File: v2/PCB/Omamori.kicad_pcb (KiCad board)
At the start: 2 copper layers, 26 x 36 mm, 12 parts, among them U1 BQ25504, U2 ATtiny13A-SSU

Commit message: Modified PCB and updated Software.
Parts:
- added D10: BPW34, own_footprints:Osram_DIL2_4.3x4.65mm_P5.08mm, F.Cu at (180.2, 91.0)
- added D11: BPW34, own_footprints:Osram_DIL2_4.3x4.65mm_P5.08mm, F.Cu at (190.2, 90.8)
- added D12: BPW34, own_footprints:Osram_DIL2_4.3x4.65mm_P5.08mm, F.Cu at (179.8, 106.8)
- added D13: BPW34, own_footprints:Osram_DIL2_4.3x4.65mm_P5.08mm, F.Cu at (187.8, 95.8)
- added D14: BPW34, own_footprints:Osram_DIL2_4.3x4.65mm_P5.08mm, F.Cu at (169.8, 111.2)
- added D15: BPW34, own_footprints:Osram_DIL2_4.3x4.65mm_P5.08mm, F.Cu at (187.8, 106.2)
- added D16: BPW34, own_footprints:Osram_DIL2_4.3x4.65mm_P5.08mm, F.Cu at (172.2, 106.2)
- added D17: BPW34, own_footprints:Osram_DIL2_4.3x4.65mm_P5.08mm, F.Cu at (177.2, 111.5)
- added D18: BPW34, own_footprints:Osram_DIL2_4.3x4.65mm_P5.08mm, F.Cu at (179.8, 91.0)
- added D19: BPW34, own_footprints:Osram_DIL2_4.3x4.65mm_P5.08mm, F.Cu at (172.2, 95.8)
- added D20: BPW34, own_footprints:Osram_DIL2_4.3x4.65mm_P5.08mm, F.Cu at (177.2, 86.2)
- added D21: BPW34, own_footprints:Osram_DIL2_4.3x4.65mm_P5.08mm, F.Cu at (182.8, 86.2)
- CSuper1: footprint Capacitor_THT:C_Rect_L7.2mm_W2.5mm_P5.00mm_FKS2_FKP2_MKS2_MKP2 -> Capacitor_THT:C_Radial_D10.0mm_H12.5mm_P5.00mm
- D1, D2, D3, D4, D5, D6, D7, D8: footprint OptoDevice:Osram_DIL2_4.3x4.65mm_P5.08mm -> own_footprints:Osram_DIL2_4.3x4.65mm_P5.08mm
- D9: footprint LED_SMD:LED_WS2812B_PLCC4_5.0x5.0mm_P3.2mm -> LED_SMD:LED_SK6812_PLCC4_5.0x5.0mm_P3.2mm
- moved D8 23.2 mm to (182.8, 111.5), turned to 0 degrees
- moved D6 11.3 mm to (190.2, 111.2), turned to 90 degrees
- moved D7 9.28 mm to (190.2, 101.0), turned to 90 degrees
- moved D3 7.52 mm to (174.8, 101.0), turned to 90 degrees
- moved D5 7.52 mm to (185.2, 101.0), turned to 90 degrees
- moved D4 4.76 mm to (180.2, 106.8), turned to 0 degrees
- moved D1 2.57 mm to (169.8, 90.8), turned to 90 degrees
- moved U2 2.30 mm to (185.2, 88.8), turned to 270 degrees
- moved D2 1.60 mm to (169.8, 101.0), turned to 90 degrees
- moved CSuper1 1.50 mm to (180.0, 101.0)
- moved D9 1.50 mm to (180.0, 98.5)
- moved U1 0.56 mm to (174.8, 87.5)
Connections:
- D1 pad 2: Net-(D1-Pad2) -> GND
- D2 pad 1: Net-(D1-Pad2) -> Net-(D1-Pad1)
- D2 pad 2: Net-(D2-Pad2) -> GND
- D3 pad 1: Net-(D2-Pad2) -> Net-(D1-Pad1)
- D3 pad 2: Net-(D3-Pad2) -> GND
- D4 pad 1: Net-(D3-Pad2) -> Net-(D1-Pad1)
- D4 pad 2: Net-(D4-Pad2) -> GND
- D5 pad 1: Net-(D4-Pad2) -> Net-(D1-Pad1)
- D5 pad 2: Net-(D5-Pad2) -> GND
- D6 pad 1: Net-(D5-Pad2) -> Net-(D1-Pad1)
- D6 pad 2: Net-(D6-Pad2) -> GND
- D7 pad 1: Net-(D6-Pad2) -> Net-(D1-Pad1)
- D7 pad 2: Net-(D7-Pad2) -> GND
- D8 pad 1: Net-(D7-Pad2) -> Net-(D1-Pad1)
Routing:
- net GND: track 26.7 -> 140.2 mm
- net Net-(CSuper1-Pad1): track 15.0 -> 0.00 mm
- net Net-(D1-Pad1): track 0.00 -> 11.6 mm
- net Net-(D5-Pad2): track 8.92 -> 0.00 mm
- net Net-(D1-Pad2): track 8.92 -> 0.00 mm
- net Net-(D7-Pad2): track 8.92 -> 0.00 mm
- net Net-(D3-Pad2): track 8.92 -> 0.00 mm
- net Net-(D6-Pad2): track 8.65 -> 0.00 mm
- net Net-(D2-Pad2): track 8.65 -> 0.00 mm
- net Net-(D4-Pad2): track 8.65 -> 0.00 mm

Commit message: Updated version 2 PCB.
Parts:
- removed the D1 at (169.8, 90.8)
- removed D10, D11, D12, D13, D14, D15, D16, D17, D18, D19, D2, D20, D21, D3, D4, D5, D6, D7, D8: BPW34, own_footprints:Osram_DIL2_4.3x4.65mm_P5.08mm
- added C_filter1: 0.1uF, Capacitor_SMD:C_0603_1608Metric_Pad1.05x0.95mm_HandSolder, B.Cu at (27.0, 24.0)
- added C_hvr1: 4.7uF, Capacitor_SMD:C_0603_1608Metric_Pad1.05x0.95mm_HandSolder, B.Cu at (32.0, 16.5)
- added C_led1: 100nF, Capacitor_SMD:C_0603_1608Metric_Pad1.05x0.95mm_HandSolder, B.Cu at (15.0, 36.0)
- added C_post_boost1: 10uF, Capacitor_SMD:C_0603_1608Metric_Pad1.05x0.95mm_HandSolder, B.Cu at (15.0, 20.0)
- added C_pre_boost1: 10uF, Capacitor_SMD:C_0603_1608Metric_Pad1.05x0.95mm_HandSolder, B.Cu at (21.0, 22.2)
- added C_ref1: 0.01uF, Capacitor_SMD:C_0603_1608Metric_Pad1.05x0.95mm_HandSolder, B.Cu at (35.0, 21.5)
- added J1: Conn_01x04_Female, Connector_PinHeader_1.27mm:PinHeader_1x04_P1.27mm_Horizontal, B.Cu at (27.0, 46.5)
- added L_boost1: 4.7uH, Inductor_SMD:L_Wuerth_MAPI-3015, B.Cu at (21.5, 18.5)
- added L_bst1: 22uH, Inductor_SMD:L_Wuerth_MAPI-3015, B.Cu at (27.8, 18.5)
- added R1: 1M, Resistor_SMD:R_0603_1608Metric_Pad1.05x0.95mm_HandSolder, B.Cu at (16.1, 17.0)
- added R_data1: 500, Resistor_SMD:R_0603_1608Metric_Pad1.05x0.95mm_HandSolder, B.Cu at (15.0, 32.5)
- added R_oc1: 3.9M, Resistor_SMD:R_0603_1608Metric_Pad1.05x0.95mm_HandSolder, B.Cu at (32.0, 19.8)
- added R_oc2: 6.2M, Resistor_SMD:R_0603_1608Metric_Pad1.05x0.95mm_HandSolder, B.Cu at (32.0, 18.0)
- added R_ok1: 2.4M, Resistor_SMD:R_0603_1608Metric_Pad1.05x0.95mm_HandSolder, B.Cu at (34.0, 29.0)
- added R_ok2: 1.6M, Resistor_SMD:R_0603_1608Metric_Pad1.05x0.95mm_HandSolder, B.Cu at (31.5, 28.0)
- added R_ok3: 6.2M, Resistor_SMD:R_0603_1608Metric_Pad1.05x0.95mm_HandSolder, B.Cu at (30.0, 28.0)
- added R_ov1: 6.2M, Resistor_SMD:R_0603_1608Metric_Pad1.05x0.95mm_HandSolder, B.Cu at (34.0, 24.5)
- added R_ov2: 3.3M, Resistor_SMD:R_0603_1608Metric_Pad1.05x0.95mm_HandSolder, B.Cu at (34.0, 23.0)
- added R_uv1: 1.6M, Resistor_SMD:R_0603_1608Metric_Pad1.05x0.95mm_HandSolder, B.Cu at (34.0, 26.0)
- added R_uv2: 8.2M, Resistor_SMD:R_0603_1608Metric_Pad1.05x0.95mm_HandSolder, B.Cu at (34.0, 27.5)
- added Sol_1: KXOB25-05X3F, own_footprints:KXOB25-05X3F, F.Cu at (33.0, 30.0)
- added Sol_2: KXOB25-05X3F, own_footprints:KXOB25-05X3F, F.Cu at (17.0, 30.0)
- added U2: TPS61222DCK, Package_TO_SOT_SMD:Texas_R-PDSO-G6, B.Cu at (18.0, 20.0)
- C_super1: renamed from CSuper1; value C -> 640mF; footprint Capacitor_THT:C_Radial_D10.0mm_H12.5mm_P5.00mm -> own_footprints:Supercap
- moved U3 179.4 mm to (17.0, 26.5), turned to 90 degrees
- moved D1 169.3 mm to (25.0, 30.5)
- moved C_super1 167.7 mm to (25.0, 37.0), turned to 180 degrees
- moved U1 158.4 mm to (30.1, 22.9), turned to 270 degrees
- renumbered D9 to D1, U2 to U3
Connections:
- D1 pad 2: Net-(D9-Pad2) -> Net-(D1-Pad2)
- D1 pad 3: Net-(D9-Pad3) -> Net-(C_led1-Pad1)
- U1 pad 15: Net-(U1-Pad15) -> Net-(C_pre_boost1-Pad1)
- U1 pad 17: Net-(U1-Pad17) -> GND
- U1 pad 5: Net-(U1-Pad5) -> GND
- U3 pad 2: Net-(U2-Pad2) -> Net-(C_led1-Pad1)
- U3 pad 5: Net-(D9-Pad2) -> Net-(R1-Pad1)
- U3 pad 6: Net-(U1-Pad11) -> Net-(J1-Pad3)
- U3 pad 7: Net-(D9-Pad3) -> Net-(J1-Pad2)
- U3 pad 8: Net-(U1-Pad15) -> Net-(C_post_boost1-Pad1)
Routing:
- net Net-(Sol_1-Pad2): track 0.00 -> 34.5 mm
- net Net-(C_post_boost1-Pad1): track 0.00 -> 34.0 mm
- net GND: track 140.2 -> 106.9 mm, vias 0 -> 5
- net Net-(J1-Pad3): track 0.00 -> 26.5 mm
- net Net-(J1-Pad2): track 0.00 -> 25.8 mm
- net Net-(C_filter1-Pad1): track 0.00 -> 20.0 mm
- net Net-(C_hvr1-Pad1): track 11.6 -> 31.0 mm, vias 0 -> 1
- net Net-(U1-Pad11): track 0.00 -> 15.5 mm, vias 0 -> 2
- net Net-(C_pre_boost1-Pad1): track 0.00 -> 14.4 mm
- net Net-(C_led1-Pad1): track 0.00 -> 13.4 mm, vias 0 -> 1
- net Net-(D1-Pad2): track 0.00 -> 11.4 mm, vias 0 -> 1
- net Net-(R_ok1-Pad1): track 0.00 -> 8.90 mm
- net Net-(R1-Pad1): track 0.00 -> 7.83 mm
- net Net-(L_boost1-Pad2): track 0.00 -> 6.20 mm
- net Net-(R_ok1-Pad2): track 0.00 -> 5.53 mm
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
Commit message: Updated PCB layout and added gerber and pictures.
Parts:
- removed R1: 1M, Resistor_SMD:R_0603_1608Metric_Pad1.05x0.95mm_HandSolder
- added D2: DIODE, Diode_SMD:D_SOD-323_HandSoldering, B.Cu at (15.5, 17.0)
- U3: value ATtiny13A-SSU -> ATtiny85
- moved C_led1 13.3 mm to (23.8, 26.0), turned to 0 degrees
- moved R_data1 9.65 mm to (23.2, 27.5), turned to 180 degrees
- moved U3 1.03 mm to (18.0, 26.8), turned to 180 degrees
- moved C_post_boost1 1.00 mm to (16.0, 20.0)
- moved C_filter1 0.90 mm to (26.2, 23.5)
- moved L_boost1 0.35 mm to (21.8, 18.8)
- moved L_bst1 0.35 mm to (27.5, 18.8), turned to 270 degrees
- moved C_pre_boost1 0.25 mm to (21.0, 22.5)
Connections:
- net Net-(C_hvr1-Pad1) renamed /Vsolar
- net Net-(C_led1-Pad1) renamed /Vcc_LED
- net Net-(C_post_boost1-Pad1) renamed /Vcc_ATTiny
- net Net-(D1-Pad2) renamed /Din_LED
- net Net-(J1-Pad2) renamed /Rx
- net Net-(J1-Pad3) renamed /Tx
- net Net-(R_data1-Pad2) renamed /Data_LED
- net Net-(R_ok1-Pad1) renamed /Vr_div
- net Net-(U1-Pad11) renamed /Vbat_ok
- C_filter1 pad 1: Net-(C_filter1-Pad1) -> /Vstor
- C_pre_boost1 pad 1: Net-(C_pre_boost1-Pad1) -> /Vstor
- C_super1 pad 1: Net-(C_filter1-Pad1) -> Net-(C_super1-Pad1)
- L_boost1 pad 1: Net-(C_pre_boost1-Pad1) -> /Vstor
- U1 pad 14: Net-(C_filter1-Pad1) -> Net-(C_super1-Pad1)
- U1 pad 15: Net-(C_pre_boost1-Pad1) -> /Vstor
- U2 pad 1: Net-(C_pre_boost1-Pad1) -> /Vstor
- U3 pad 5: Net-(R1-Pad1) -> /Vsolar_measure
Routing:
- net Net-(C_filter1-Pad1): track 20.0 -> 0.00 mm
- net Net-(C_super1-Pad1): track 0.00 -> 17.1 mm
- net Net-(C_pre_boost1-Pad1): track 14.4 -> 0.00 mm
- net /Vstor: track 0.00 -> 14.0 mm
- net /Vsolar_measure: track 0.00 -> 13.4 mm
- net /Din_LED: track 11.4 -> 3.20 mm
- net Net-(R1-Pad1): track 7.83 -> 0.00 mm
- net GND: track 106.9 -> 112.0 mm, vias 5 -> 6
- net /Vsolar: track 31.0 -> 27.8 mm
- net /Tx: track 26.5 -> 23.4 mm
- net /Vcc_LED: track 13.4 -> 15.9 mm
- net /Vcc_ATTiny: track 34.0 -> 35.9 mm
- net Net-(L_boost1-Pad2): track 6.20 -> 4.59 mm
- net /Data_LED: track 3.49 -> 1.95 mm
- net Net-(Sol_1-Pad2): track 34.5 -> 33.7 mm
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
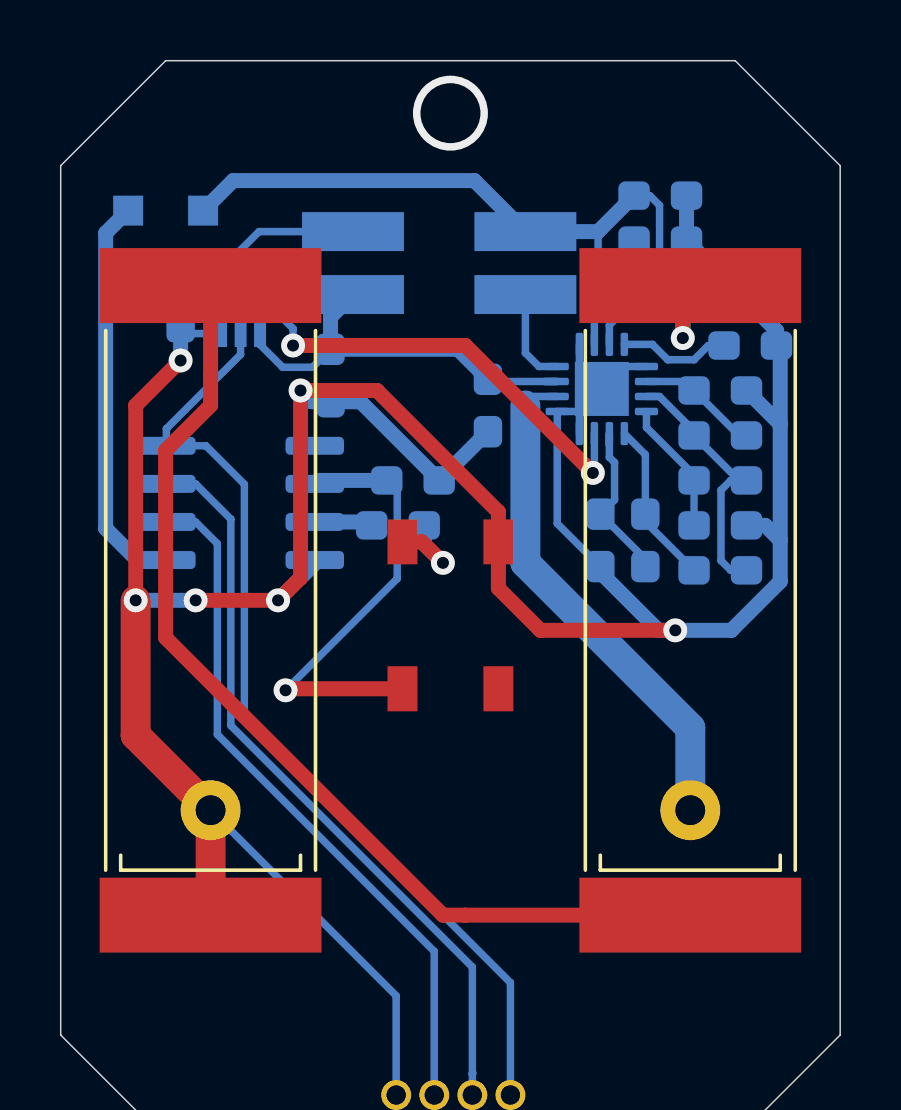
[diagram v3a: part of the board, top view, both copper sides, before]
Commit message: Thickened a lot of wires and ordered stuff a bit.
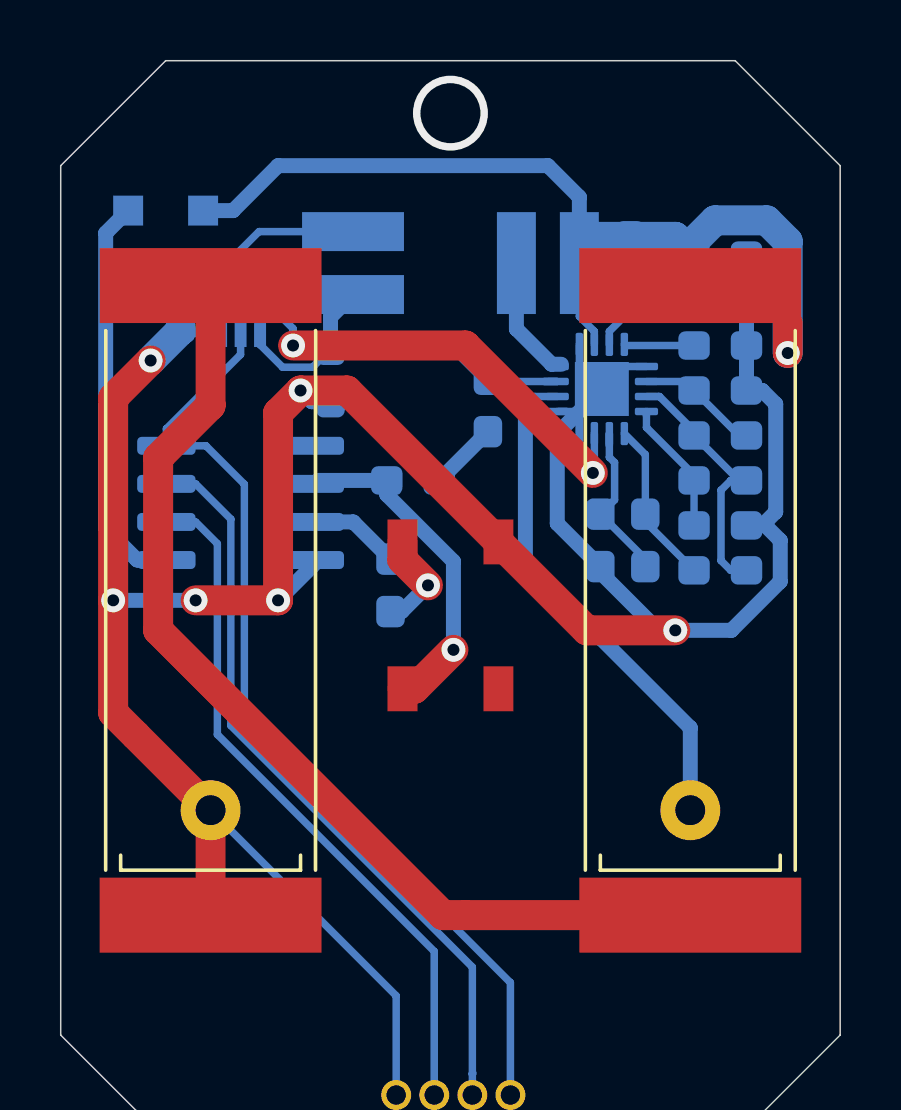
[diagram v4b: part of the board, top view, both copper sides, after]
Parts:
- moved C_hvr1 2.83 mm to (34.0, 18.5)
- moved R_oc2 2.83 mm to (34.0, 20.0)
- moved R_data1 2.02 mm to (23.0, 29.5), turned to 90 degrees
- moved R_oc1 1.41 mm to (31.0, 18.8), turned to 270 degrees
- moved C_ref1 1.00 mm to (34.0, 21.5)
- moved L_bst1 0.75 mm to (28.2, 18.8), turned to 180 degrees
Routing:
- net GND: track 112.0 -> 108.3 mm
- net /Vsolar: track 27.8 -> 31.4 mm
- net /Vcc_LED: track 15.9 -> 12.6 mm
- net Net-(C_ref1-Pad1): track 3.79 -> 2.34 mm
- net /Data_LED: track 1.95 -> 3.04 mm
- net Net-(L_bst1-Pad2): track 3.20 -> 4.19 mm

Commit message: Changed resistor position to make supercap fit.
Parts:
- moved C_led1 1.60 mm to (22.5, 25.0), turned to 90 degrees
- moved R_data1 1.58 mm to (23.5, 28.0), turned to 180 degrees
- moved Sol_1 0.25 mm to (32.8, 30.0)
- moved Sol_2 0.25 mm to (17.2, 30.0)
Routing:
- net /Vsolar: track 31.4 -> 34.4 mm
- net GND: track 108.3 -> 106.9 mm
- net /Data_LED: track 3.04 -> 2.40 mm
- net /Vcc_LED: track 12.6 -> 13.1 mm
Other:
- board size 26 x 36 mm -> 25 x 35 mm

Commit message: I am not sure what changed to be honest.
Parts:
- moved Sol_1 0.50 mm to (33.2, 30.0)
- moved Sol_2 0.50 mm to (16.8, 30.0)

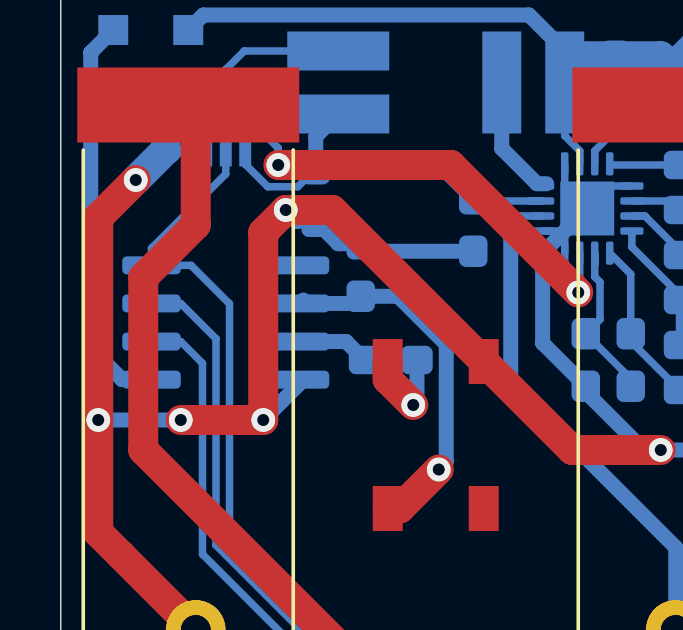
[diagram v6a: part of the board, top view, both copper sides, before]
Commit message: Added a really ugly GND Polygon.
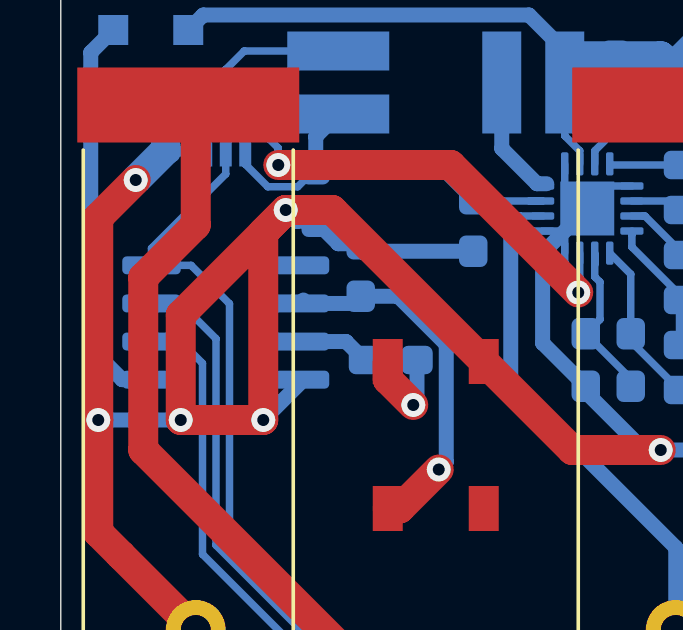
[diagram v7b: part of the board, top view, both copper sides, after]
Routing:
- net GND: track 106.9 -> 115.4 mm
- added copper zone on F.Cu, net GND

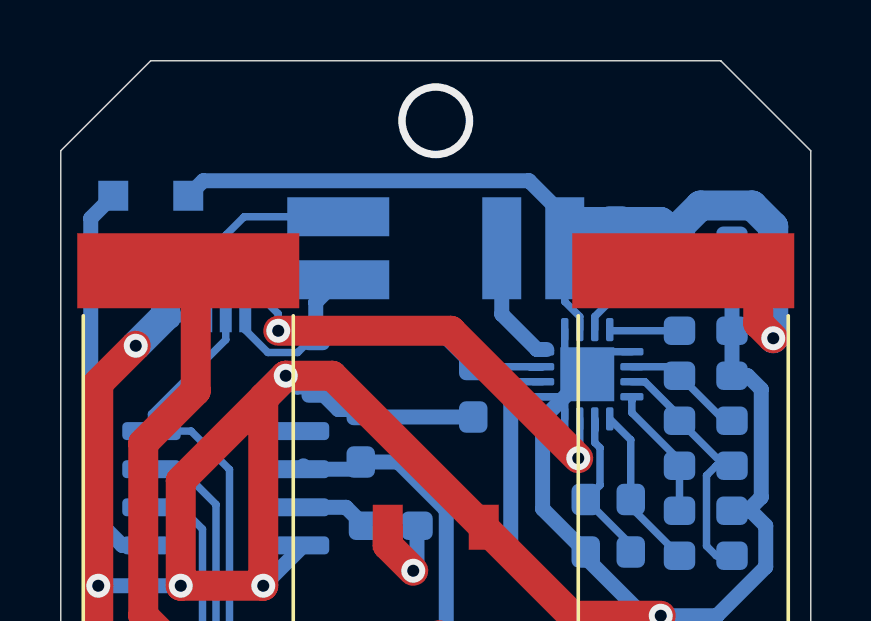
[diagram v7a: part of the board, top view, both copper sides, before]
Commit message: Datasheet and description update as well as other minor design changes.
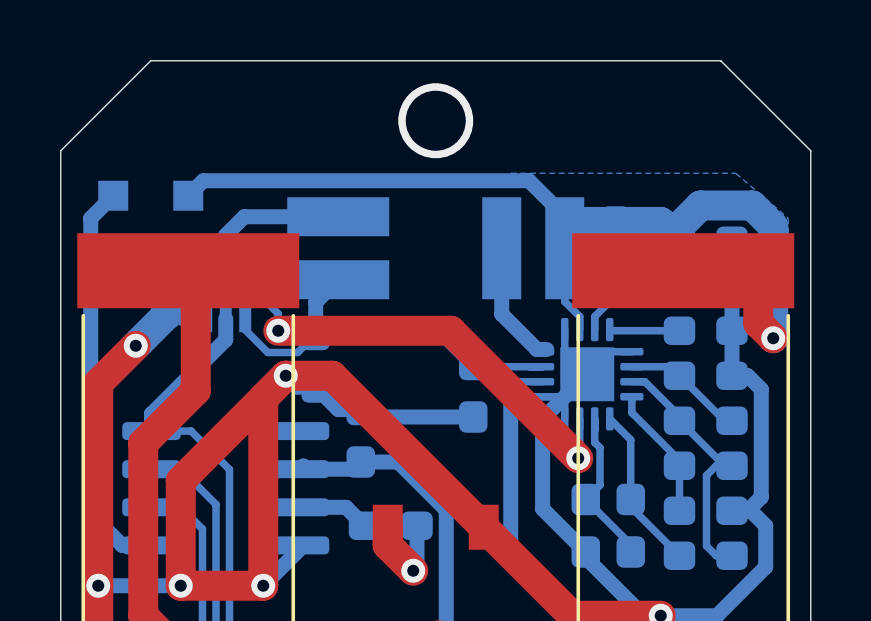
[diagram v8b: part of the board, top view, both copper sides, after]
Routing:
- added copper zone on B.Cu, net /Vsolar
